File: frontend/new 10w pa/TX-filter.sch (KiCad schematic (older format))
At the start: 60 parts, among them K2 D3002, K3 D3002, K4 D3002, K5 D3002, K6 D3002, K7 D3002, Q4 2N7000, Q5 2N7000, Q6 2N7000, Q7 2N7000, Q8 2N7000, Q9 2N7000, U1 4028

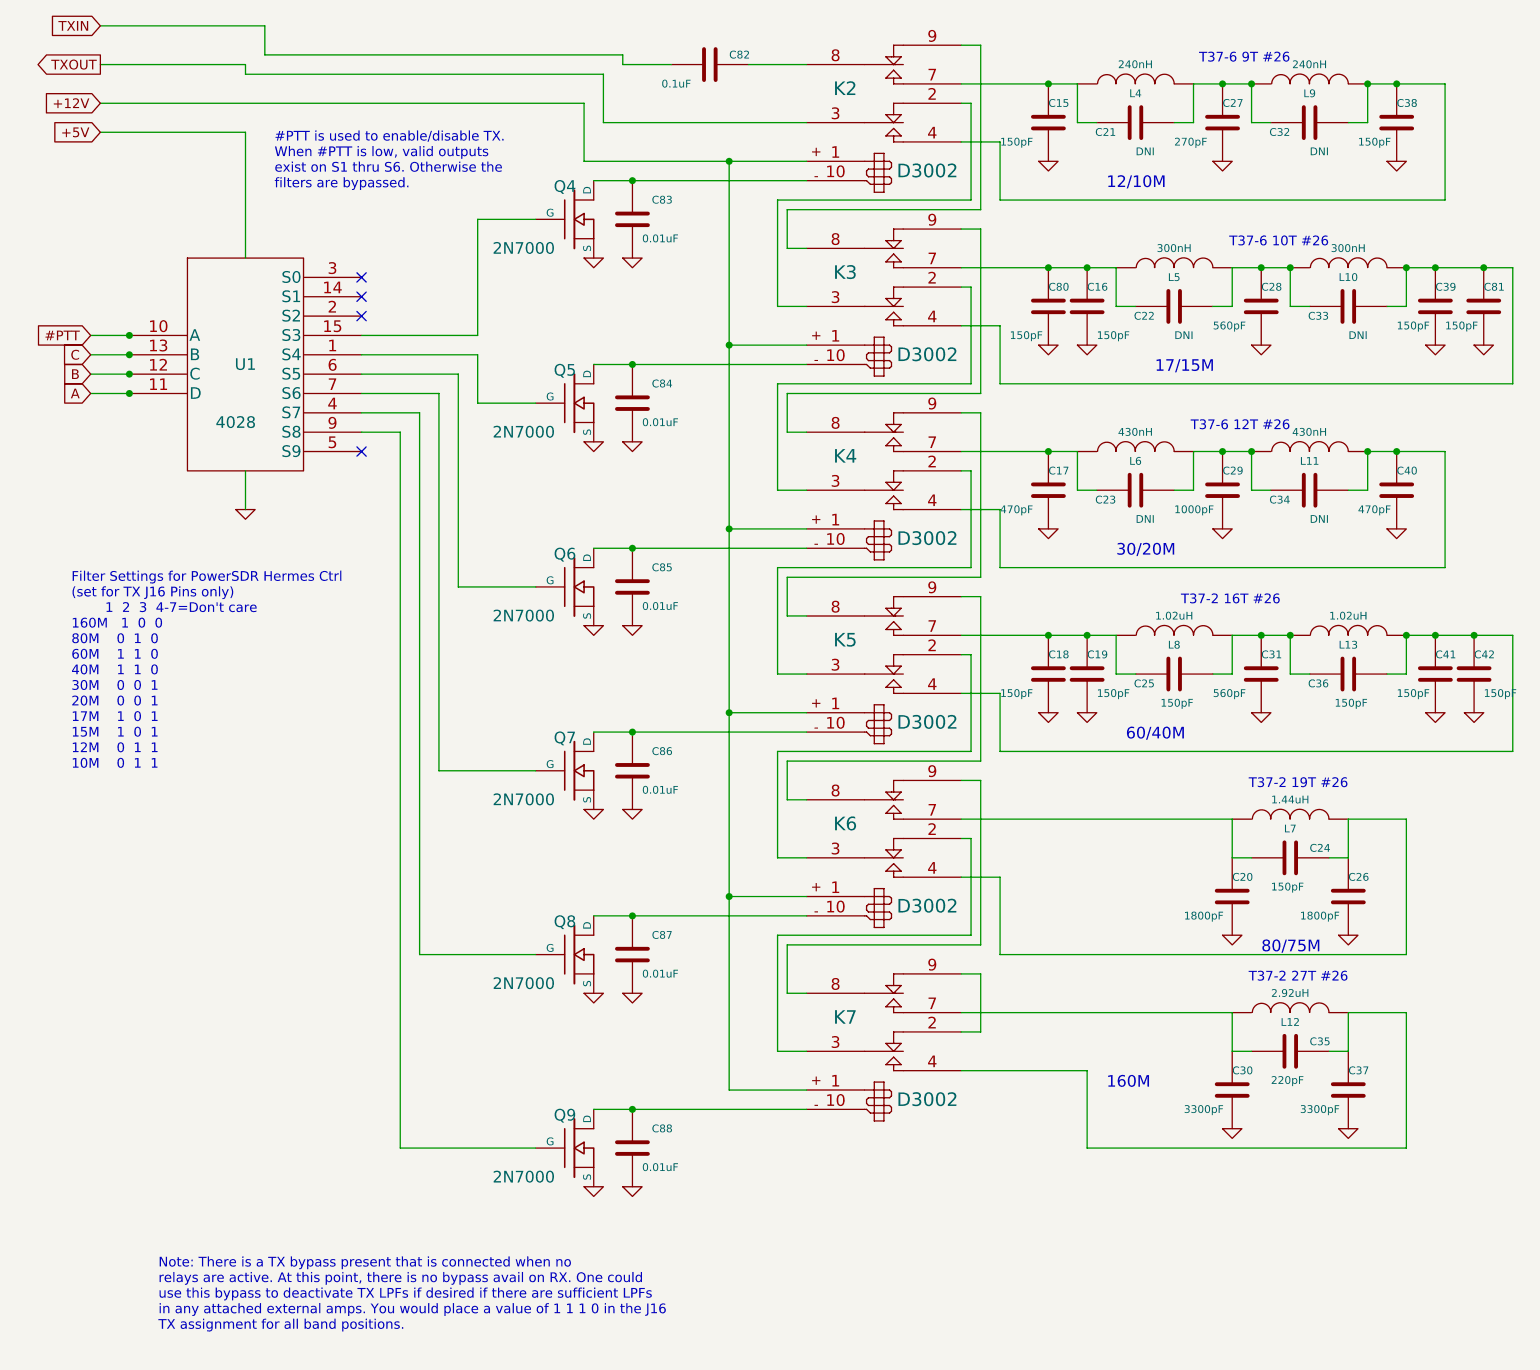
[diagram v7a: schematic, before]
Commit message: Changes for new J16 approach
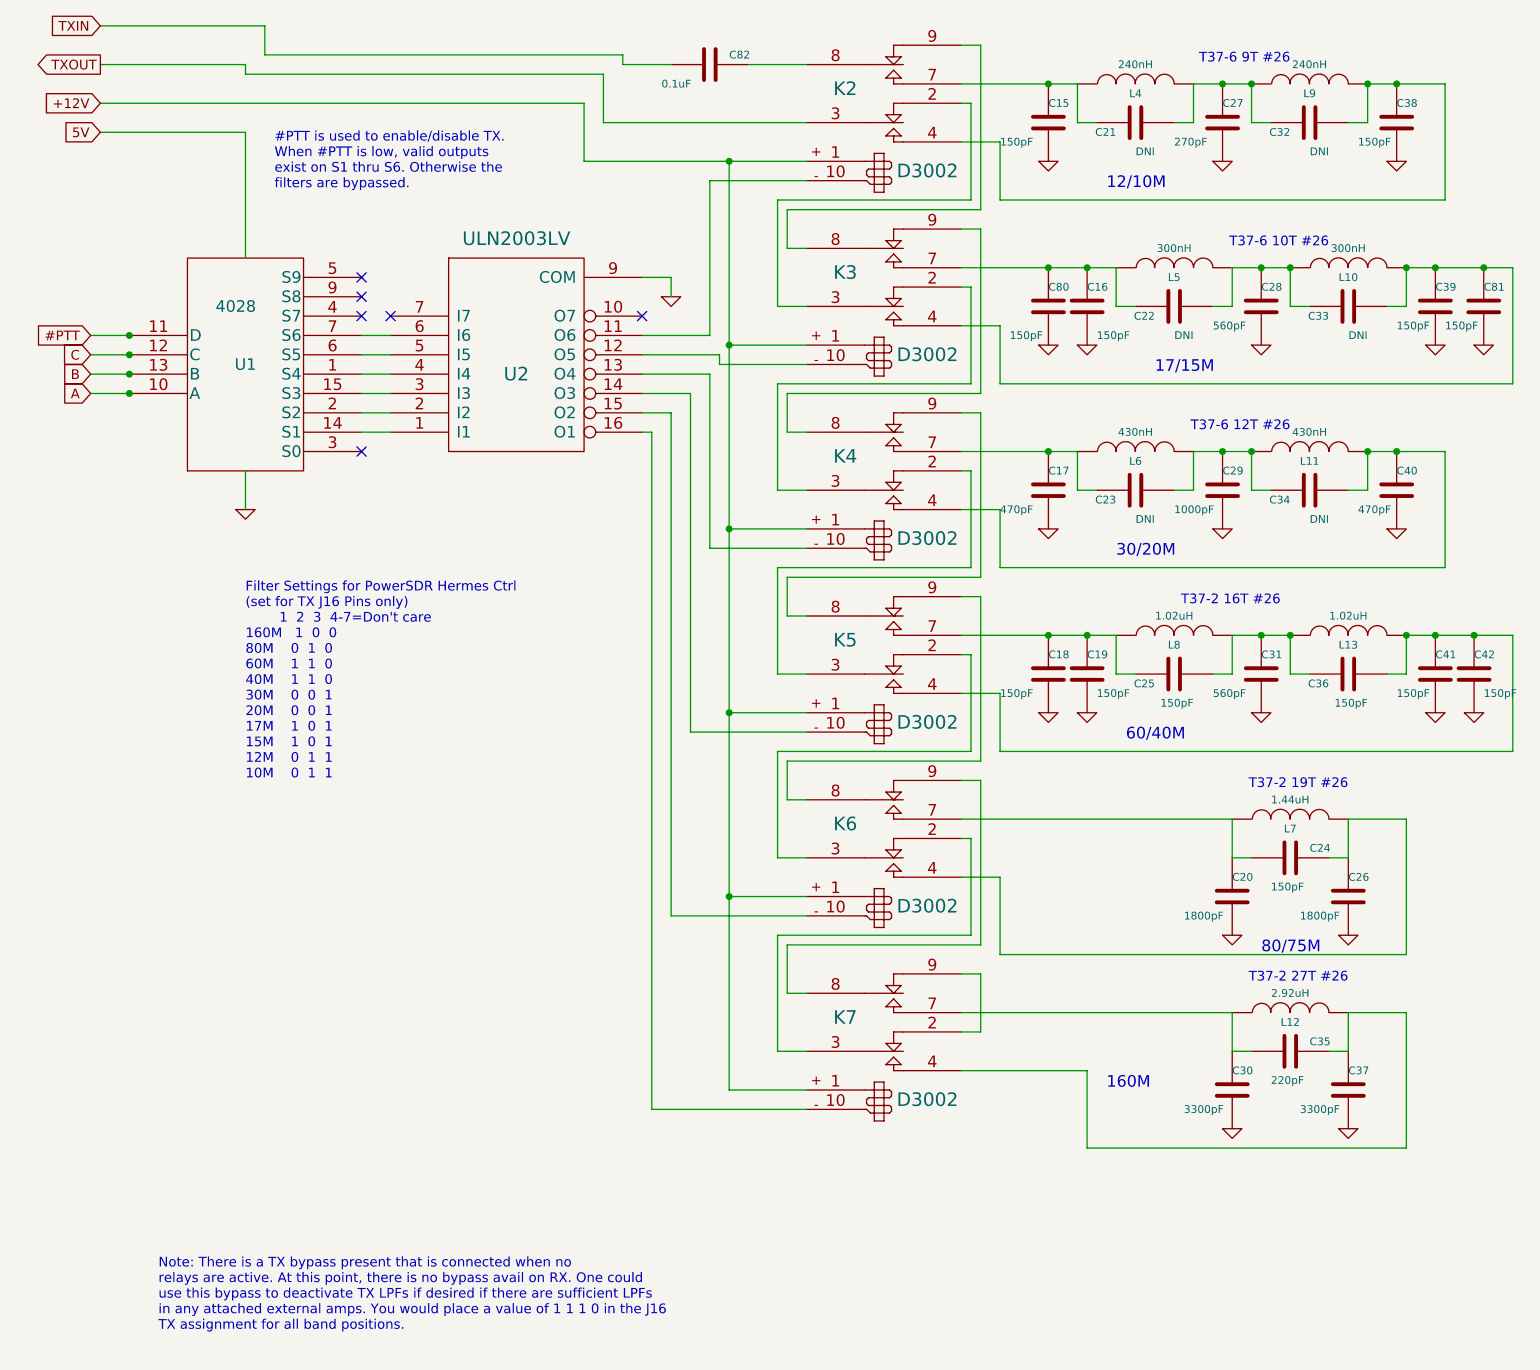
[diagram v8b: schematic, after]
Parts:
- removed C83, C84, C85, C86, C87, C88: 0.01uF, HERMESLITE:C_0805, symbol C
- removed Q4, Q5, Q6, Q7, Q8, Q9: 2N7000, SMD_Packages:SOT-23-GDS, symbol MOSFET_N
- added U2: ULN2003LV, SMD_Packages:TSSOP-16, symbol ULN2003A
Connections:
- net VDD is gone; now on net GND: U1.16 (VDD)
- net #PTT: now also U1.11 (D); no longer U1.10 (A)
- net A: now also U1.10 (A); no longer U1.11 (D)
- net B: now also U1.13 (B); no longer U1.12 (C)
- net C: now also U1.12 (C); no longer U1.13 (B)
- net GND: now also U2.8 (GND), U2.9 (COM); no longer U1.8 (VSS)
- net at K2.10 (-): now also U2.11 (O6)
- net at K3.10 (-): now also U2.12 (O5)
- net at K4.10 (-): now also U2.13 (O4)
- net at K5.10 (-): now also U2.14 (O3)
- net at K6.10 (-): now also U2.15 (O2)
- net at K7.10 (-): now also U2.16 (O1)
- net at U1.7 (S6): now also U2.6 (I6)
- net at U1.6 (S5): now also U2.5 (I5)
- net at U1.1 (S4): now also U2.4 (I4)
- net at U1.15 (S3): now also U2.3 (I3)
- net at U1.14 (S1): now also U2.1 (I1)
- net at U1.2 (S2): now also U2.2 (I2)
- new net VSS: U1.8 (VSS)
- no-connect marks 4 -> 6
